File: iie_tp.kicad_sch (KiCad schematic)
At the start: 47 parts, among them J1 Conn_01x03, J2 Conn_01x02, J3 Conn_01x01, J4 Conn_01x01, J5 Conn_01x02, J6 Conn_01x02, J7 Conn_01x03, J8 AudioJack2_Ground, U1 ${SIM.PARAMS}, U2 LM386

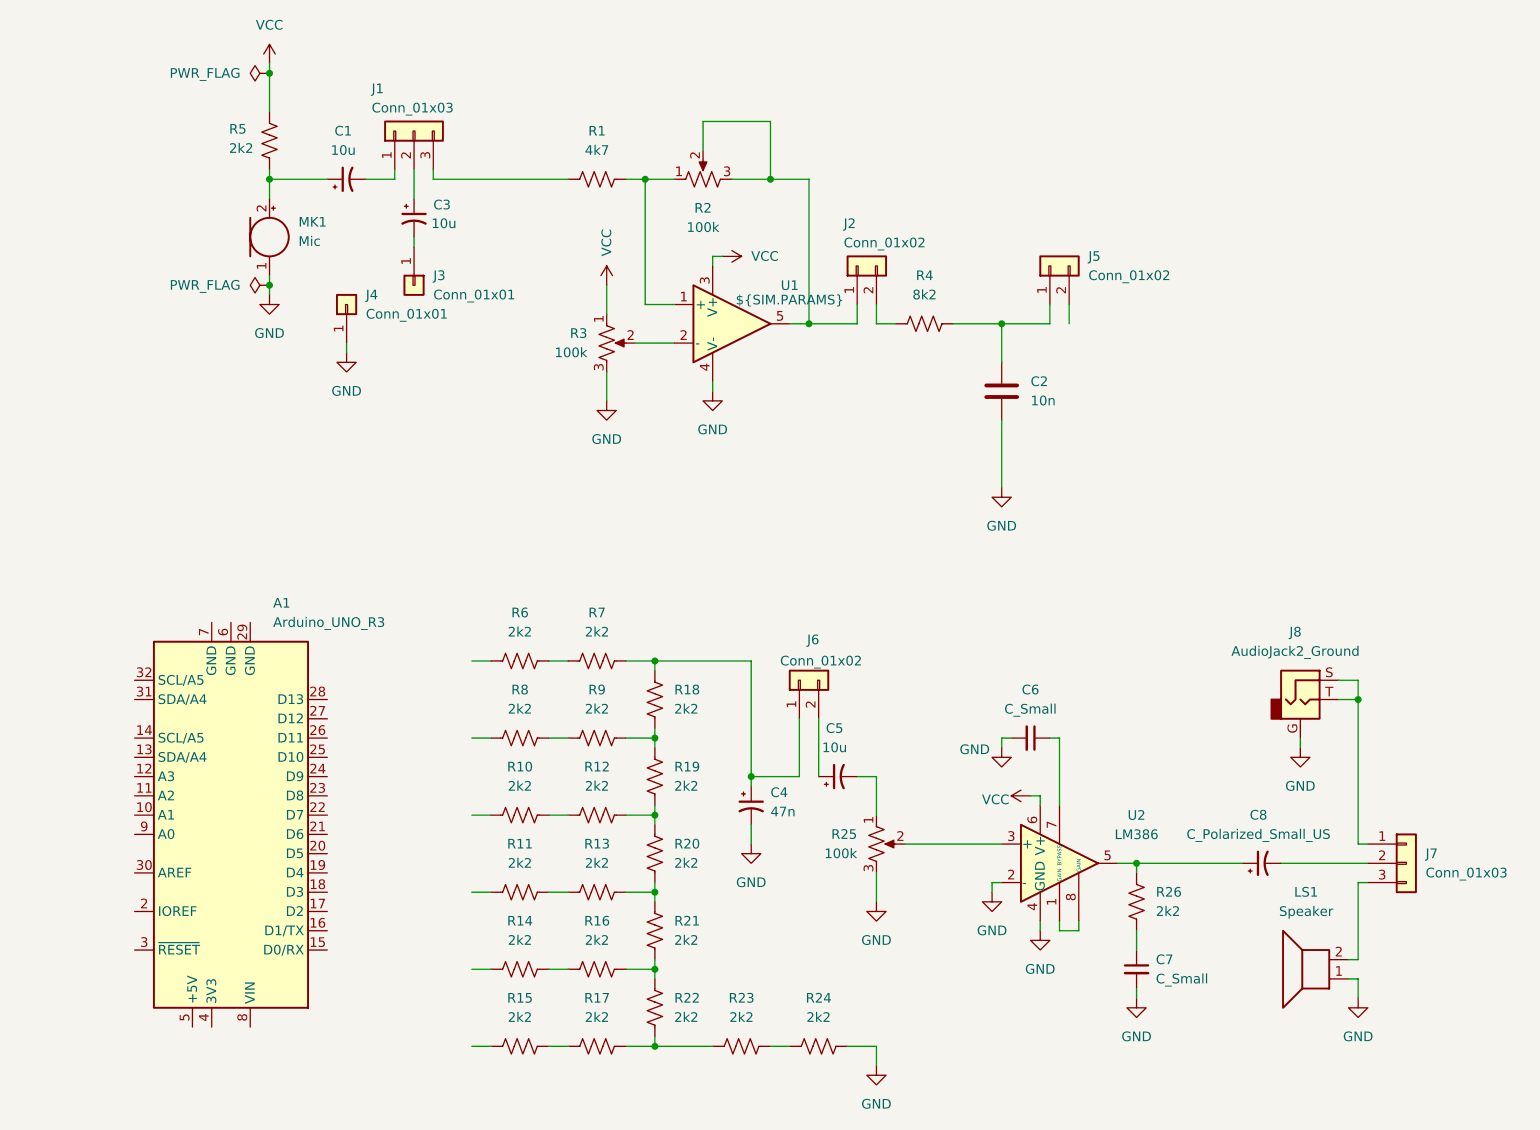
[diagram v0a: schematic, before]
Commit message: feat: Conecto los pines de salida del arduino al ADC
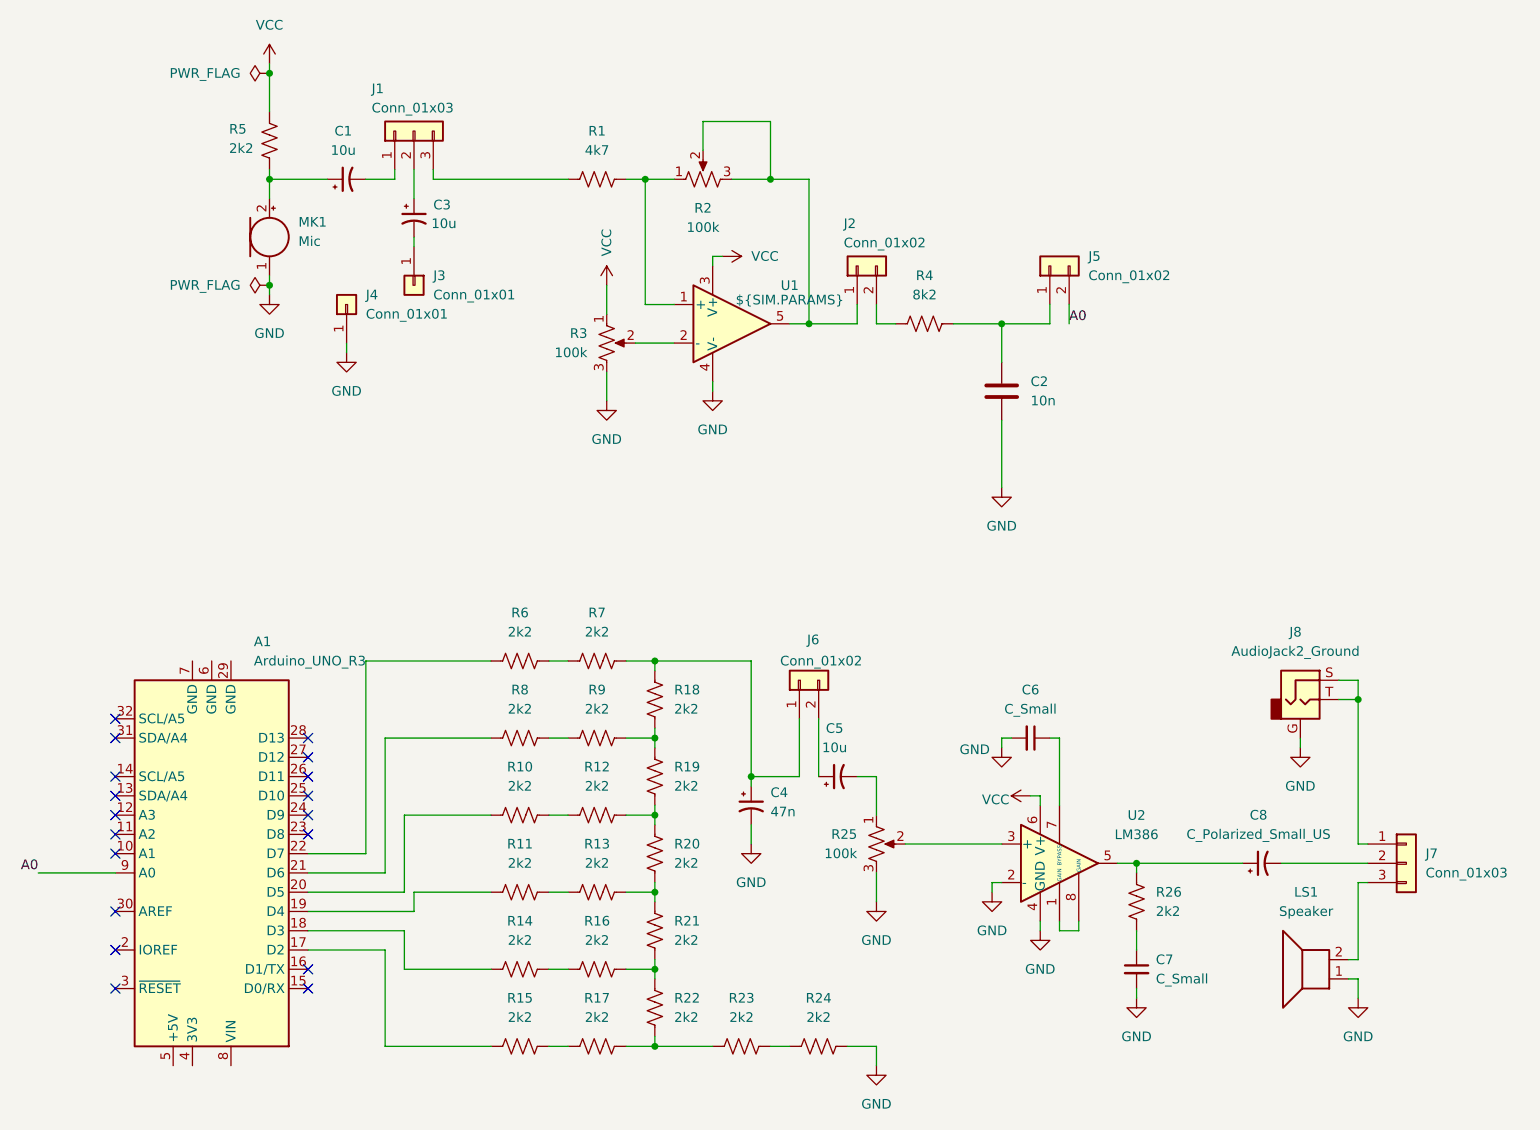
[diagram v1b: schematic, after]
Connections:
- net at A1.17 (D2): now also R15.2
- net at A1.18 (D3): now also R14.1
- net at A1.19 (D4): now also R11.2
- net at A1.20 (D5): now also R10.1
- net at A1.21 (D6): now also R8.2
- net at A1.22 (D7): now also R6.1
- net A0: now reaches A1.9 (A0)
- net A0: now also J5.2 (Pin_2)
- no-connect marks 0 -> 18
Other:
- moved on the sheet: A1
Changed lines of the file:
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@@
 (kicad_sch
-	(version 20231120)
+	(version 20250114)
 	(generator "eeschema")
-	(generator_version "8.0")
+	(generator_version "9.0")
 	(paper "A4")
 	(junction
@@
 		(color 0 0 0 0)
 	)
+	(no_connect
+		(at 59.69 129.54)
+	)
+	(no_connect
+		(at 59.69 149.86)
+	)
+	(no_connect
+		(at 34.29 132.08)
+	)
+	(no_connect
+		(at 59.69 119.38)
+	)
+	(no_connect
+		(at 34.29 144.78)
+	)
+	(no_connect
+		(at 34.29 149.86)
+	)
+	(no_connect
+		(at 34.29 129.54)
+	)
+	(no_connect
+		(at 59.69 147.32)
+	)
+	(no_connect
+		(at 34.29 116.84)
+	)
+	(no_connect
+		(at 34.29 114.3)
+	)
+	(no_connect
+		(at 34.29 127)
+	)
+	(no_connect
+		(at 59.69 116.84)
+	)
+	(no_connect
+		(at 34.29 121.92)
+	)
+	(no_connect
+		(at 34.29 139.7)
+	)
+	(no_connect
+		(at 59.69 127)
+	)
+	(no_connect
+		(at 34.29 124.46)
+	)
+	(no_connect
+		(at 59.69 124.46)
+	)
+	(no_connect
+		(at 59.69 121.92)
+	)
 	(wire
 		(pts
@@
 	(wire
 		(pts
+			(xy 72.39 142.24) (xy 59.69 142.24)
+		)
+		(stroke
+			(width 0)
+			(type default)
+		)
+	)
+	(wire
+		(pts
 			(xy 158.75 142.24) (xy 161.29 142.24)
 		)
@@
 	(wire
 		(pts
-			(xy 81.28 137.16) (xy 83.82 137.16)
+			(xy 24.13 134.62) (xy 34.29 134.62)
+		)
+		(stroke
+			(width 0)
+			(type default)
+		)
+	)
+	(wire
+		(pts
+			(xy 69.85 116.84) (xy 83.82 116.84)
 		)
 		(stroke
@@
 	(wire
 		(pts
-			(xy 81.28 116.84) (xy 83.82 116.84)
+			(xy 69.85 144.78) (xy 69.85 157.48)
+		)
+		(stroke
+			(width 0)
+			(type default)
+		)
+	)
+	(wire
+		(pts
+			(xy 67.31 106.68) (xy 67.31 132.08)
+		)
+		(stroke
+			(width 0)
+			(type default)
+		)
+	)
+	(wire
+		(pts
+			(xy 67.31 106.68) (xy 83.82 106.68)
 		)
 		(stroke
@@
 	(wire
 		(pts
+			(xy 59.69 144.78) (xy 69.85 144.78)
+		)
+		(stroke
+			(width 0)
+			(type default)
+		)
+	)
+	(wire
+		(pts
 			(xy 91.44 137.16) (xy 93.98 137.16)
 		)
@@
 	(wire
 		(pts
-			(xy 81.28 106.68) (xy 83.82 106.68)
+			(xy 59.69 134.62) (xy 69.85 134.62)
+		)
+		(stroke
+			(width 0)
+			(type default)
+		)
+	)
+	(wire
+		(pts
+			(xy 73.66 137.16) (xy 73.66 139.7)
 		)
 		(stroke
@@
 	(wire
 		(pts
+			(xy 73.66 139.7) (xy 59.69 139.7)
+		)
+		(stroke
+			(width 0)
+			(type default)
+		)
+	)
+	(wire
+		(pts
+			(xy 72.39 147.32) (xy 72.39 142.24)
+		)
+		(stroke
+			(width 0)
+			(type default)
+		)
+	)
+	(wire
+		(pts
 			(xy 105.41 137.16) (xy 105.41 138.43)
 		)
@@
 	(wire
 		(pts
+			(xy 73.66 137.16) (xy 83.82 137.16)
+		)
+		(stroke
+			(width 0)
+			(type default)
+		)
+	)
+	(wire
+		(pts
+			(xy 59.69 137.16) (xy 72.39 137.16)
+		)
+		(stroke
+			(width 0)
+			(type default)
+		)
+	)
+	(wire
+		(pts
+			(xy 69.85 157.48) (xy 83.82 157.48)
+		)
+		(stroke
+			(width 0)
+			(type default)
+		)
+	)
+	(wire
+		(pts
 			(xy 91.44 106.68) (xy 93.98 106.68)
 		)
@@
 	(wire
 		(pts
+			(xy 67.31 132.08) (xy 59.69 132.08)
+		)
+		(stroke
+			(width 0)
+			(type default)
+		)
+	)
+	(wire
+		(pts
 			(xy 120.65 43.18) (xy 125.73 43.18)
 		)
@@
 	(wire
 		(pts
+			(xy 72.39 127) (xy 83.82 127)
+		)
+		(stroke
+			(width 0)
+			(type default)
+		)
+	)
+	(wire
+		(pts
 			(xy 105.41 156.21) (xy 105.41 157.48)
 		)
@@
 	(wire
 		(pts
-			(xy 81.28 147.32) (xy 83.82 147.32)
+			(xy 72.39 137.16) (xy 72.39 127)
 		)
 		(stroke
@@
 	(wire
 		(pts
-			(xy 81.28 127) (xy 83.82 127)
-		)
-		(stroke
-			(width 0)
-			(type default)
-		)
-	)
-	(wire
-		(pts
 			(xy 120.65 157.48) (xy 123.19 157.48)
 		)
@@
 	(wire
 		(pts
+			(xy 69.85 134.62) (xy 69.85 116.84)
+		)
+		(stroke
+			(width 0)
+			(type default)
+		)
+	)
+	(wire
+		(pts
 			(xy 198.12 148.59) (xy 196.85 148.59)
 		)
@@
 	(wire
 		(pts
-			(xy 111.76 35.56) (xy 120.65 35.56)
+			(xy 72.39 147.32) (xy 83.82 147.32)
 		)
 		(stroke
@@
 	(wire
 		(pts
-			(xy 54.61 43.18) (xy 62.23 43.18)
+			(xy 111.76 35.56) (xy 120.65 35.56)
 		)
 		(stroke
@@
 	(wire
 		(pts
-			(xy 134.62 121.92) (xy 132.08 121.92)
+			(xy 54.61 43.18) (xy 62.23 43.18)
 		)
 		(stroke
@@
 	(wire
 		(pts
-			(xy 76.2 41.91) (xy 76.2 43.18)
+			(xy 134.62 121.92) (xy 132.08 121.92)
 		)
 		(stroke
@@
 	(wire
 		(pts
-			(xy 104.14 43.18) (xy 107.95 43.18)
+			(xy 76.2 41.91) (xy 76.2 43.18)
 		)
 		(stroke
@@
 	(wire
 		(pts
-			(xy 118.11 106.68) (xy 118.11 121.92)
+			(xy 104.14 43.18) (xy 107.95 43.18)
 		)
 		(stroke
@@
 	(wire
 		(pts
-			(xy 151.13 118.11) (xy 151.13 116.84)
+			(xy 118.11 106.68) (xy 118.11 121.92)
 		)
 		(stroke
@@
 	(wire
 		(pts
-			(xy 118.11 130.81) (xy 118.11 128.27)
+			(xy 151.13 118.11) (xy 151.13 116.84)
 		)
 		(stroke
@@
 	(wire
 		(pts
-			(xy 81.28 157.48) (xy 83.82 157.48)
+			(xy 118.11 130.81) (xy 118.11 128.27)
 		)
 		(stroke
@@
 		)
 	)
+	(label "A0"
+		(at 160.02 62.23 0)
+		(effects
+			(font
+				(size 1.27 1.27)
+			)
+			(justify left bottom)
+		)
+	)
+	(label "A0"
+		(at 24.13 134.62 180)
+		(effects
+			(font
+				(size 1.27 1.27)
+			)
+			(justify right bottom)
+		)
+	)
 	(symbol
 		(lib_id "Device:C_Polarized_Small_US")
@@
 	(symbol
 		(lib_id "MCU_Module:Arduino_UNO_R3")
-		(at 49.53 129.54 180)
+		(at 46.99 134.62 180)
 		(unit 1)
 		(exclude_from_sim no)
@@
 		(fields_autoplaced yes)
 		(property "Reference" "A1"
-			(at 55.0865 99.06 0)
+			(at 52.5465 104.14 0)
 			(effects
 				(font
@@
 		)
 		(property "Value" "Arduino_UNO_R3"
-			(at 55.0865 101.6 0)
+			(at 52.5465 106.68 0)
 			(effects
 				(font
@@
 		)
 		(property "Footprint" "Module:Arduino_UNO_R3"
-			(at 49.53 129.54 0)
+			(at 46.99 134.62 0)
 			(effects
 				(font
@@
 		)
 		(property "Datasheet" "https://www.arduino.cc/en/Main/arduinoBoardUno"
-			(at 49.53 129.54 0)
+			(at 46.99 134.62 0)
 			(effects
 				(font
@@
 		)
 		(property "Description" "Arduino UNO Microcontroller Module, release 3"
-			(at 49.53 129.54 0)
+			(at 46.99 134.62 0)
 			(effects
 				(font
@@
 		)
 	)
+	(embedded_fonts no)
 )
